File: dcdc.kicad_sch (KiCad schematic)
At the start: 198 parts, among them U11 SIC437AED-T1-GE3, U12 SIC437AED-T1-GE3, U13 SIC437AED-T1-GE3, U22 INA219AIDCNR, U50 INA219AIDCNR, U60 INA219AIDCNR, U65 SIC437AED-T1-GE3, U66 INA219AIDCNR, U69 TPS564247DRLR, U7 TPS564247DRLR, U75 SIC437AED-T1-GE3, U76 INA219AIDCNR, U8 SIC437AED-T1-GE3

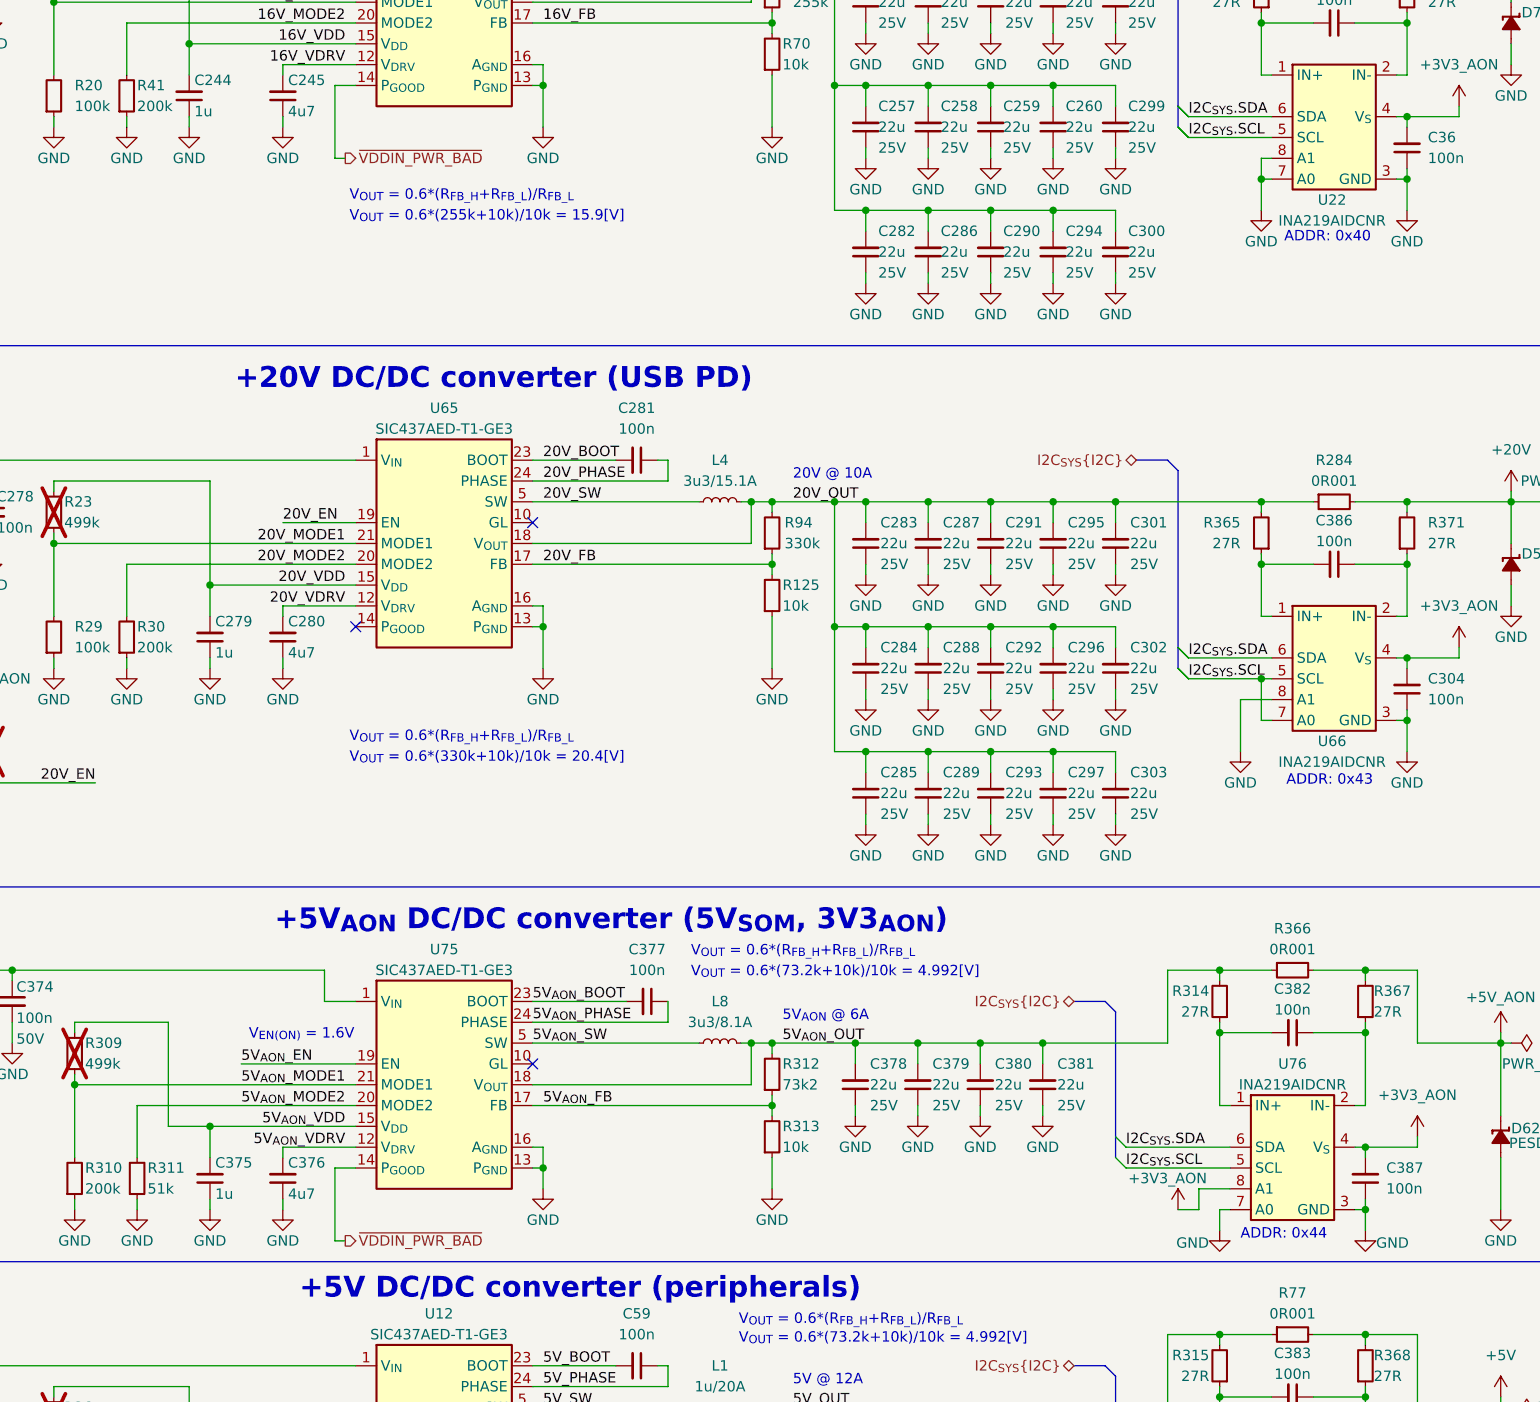
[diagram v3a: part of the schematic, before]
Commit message: [#90793] Change R311 to 100k, replace L8 to Bourns SRP7028A-3R3M, re-route 5V_AON DC-DC area, change power monitors I2C addresses 0x40 > 0x45 and 0x44 > 0x46
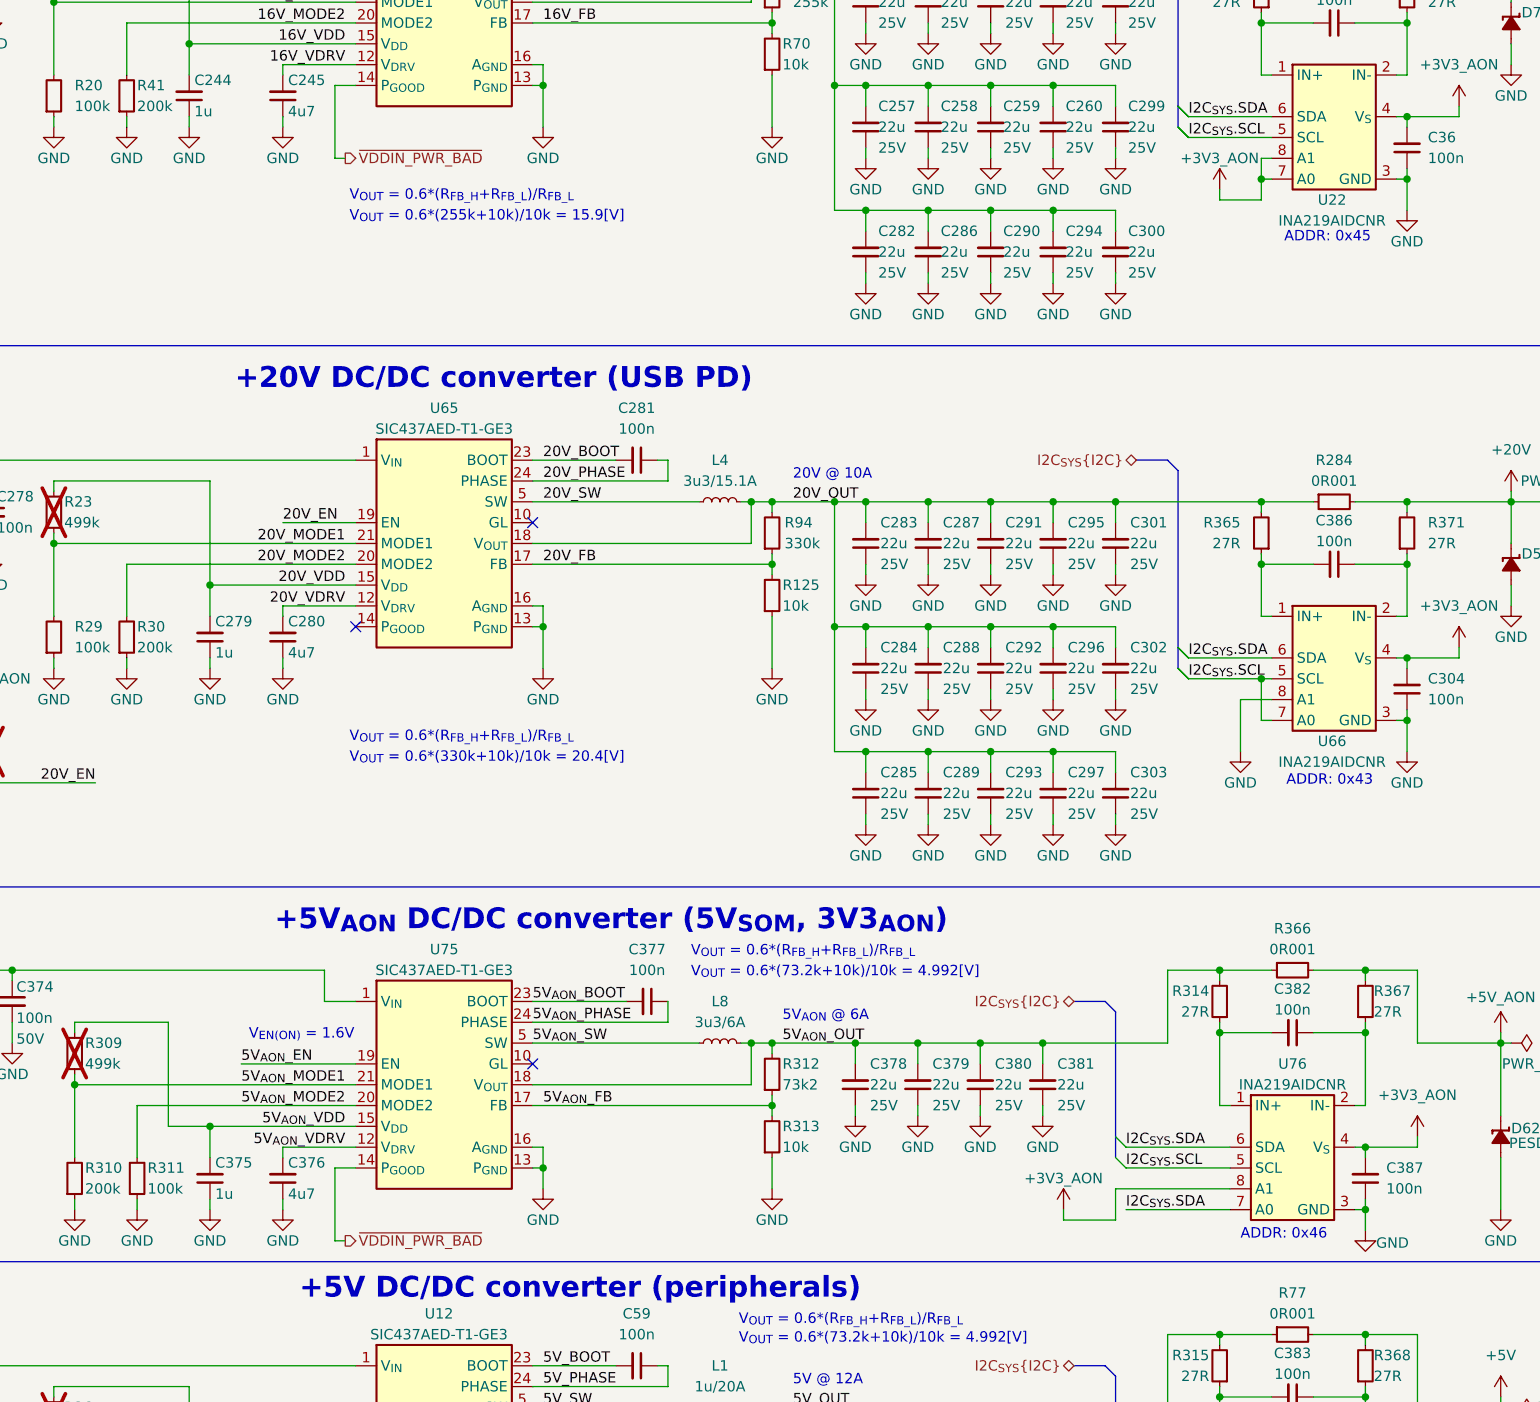
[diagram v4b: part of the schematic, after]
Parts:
- removed L8: L_3u3_8.1A_Coilcraft-XAL5030, antmicro-footprints:L_Coilcraft-XAL5030, symbol antmicroFixedInductors:L_3u3_8.1A_Coilcraft-XAL5030
- removed R311: R_51k_0402, antmicro-footprints:R_0402_1005Metric, symbol antmicroResistors0402:R_51k_0402
- added L8: L_3u3_6A_Bourns-SRP7028A, antmicro-footprints:L_Bourns-SRP7028A, symbol antmicroFixedInductors:L_3u3_6A_Bourns-SRP7028A
- added R311: R_100k_0402, antmicro-footprints:R_0402_1005Metric, symbol antmicroResistors0402:R_100k_0402
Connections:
- net +3V3_AON: now also U22.7 (A0), U22.8 (A1)
- net 5V_{AON}_MODE2: now also R311.2
- net 5V_{AON}_OUT: now also L8.2
- net 5V_{AON}_SW: now also L8.1
- net GND: now also R311.1; no longer U22.7 (A0), U22.8 (A1), U76.7 (A0)
- net I2C_{SYS}.SDA: now also U76.7 (A0)
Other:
- note added: "ADDR: 0x45"
- note added: "ADDR: 0x46"
- note removed: "ADDR: 0x40"
- note removed: "ADDR: 0x44"
